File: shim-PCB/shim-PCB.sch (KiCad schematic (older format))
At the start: 23 parts, among them J1 ROMI-Encoder, J10 LineSensor, J11 LineSensor, J12 SPI, J13 Ultrasonic., J14 THING, J15 THING, J16 Conn_01x02_Female, J2 ROMI-Encoder, J3 Conn_01x19_Female, J4 ServoAnalog, J5 Conn_01x19_Female, J6 Conn_01x19_Female, J7 ROMI, J8 ROMI, J9 Conn_01x19_Female

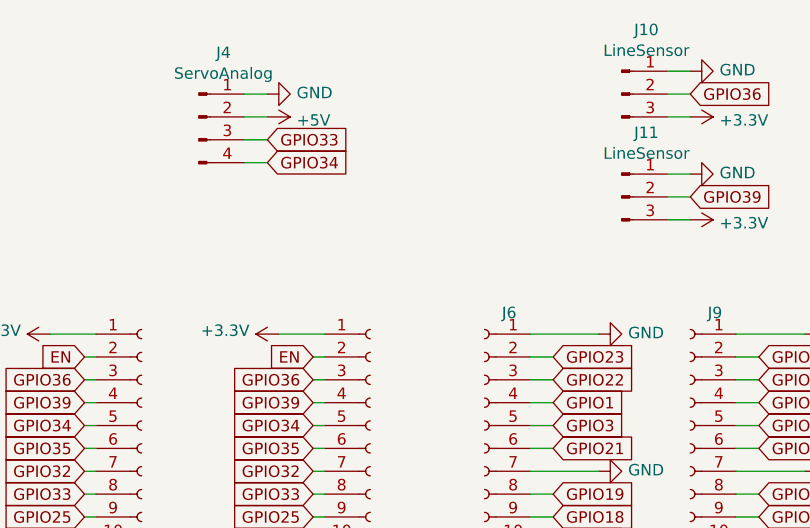
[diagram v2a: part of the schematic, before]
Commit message: Clamped analog input signal.
Fixed issue #11
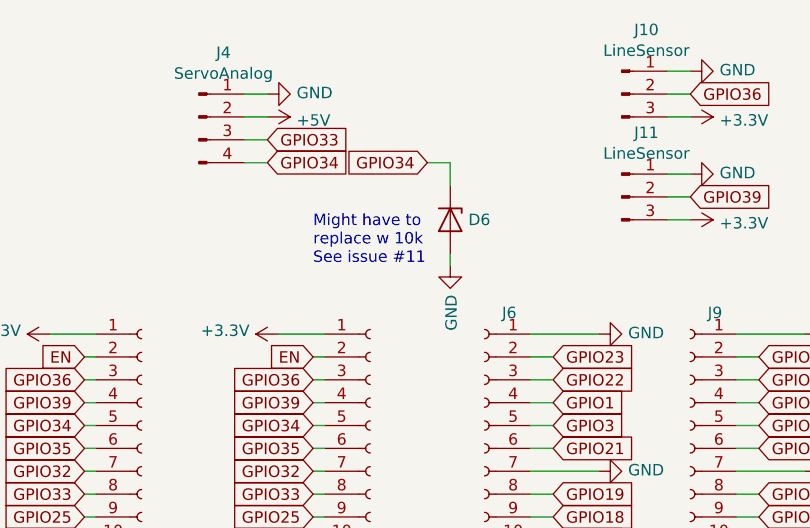
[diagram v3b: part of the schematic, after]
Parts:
- added D6: D_Zener, Diode_THT:D_DO-35_SOD27_P7.62mm_Horizontal, symbol Device:D_Zener
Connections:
- net GND: now also D6.2 (A)
- net GPIO34: now also D6.1 (K)
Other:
- note added: "Might have to\nreplace w 10k\nSee issue #11"
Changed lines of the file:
@@
 Wire Wire Line
 	4800 4650 4800 4700
+$Comp
+L Device:D_Zener D6
+U 1 1 5F32D98F
+P 2850 1550
+F 0 "D6" V 2850 1629 50  0000 L CNN
+F 1 "D_Zener" V 2895 1629 50  0001 L CNN
+F 2 "Diode_THT:D_DO-35_SOD27_P7.62mm_Horizontal" H 2850 1550 50  0001 C CNN
+F 3 "~" H 2850 1550 50  0001 C CNN
+	1    2850 1550
+	0    1    1    0
+$EndComp
+Text GLabel 2750 1300 0    50   Input ~ 0
+GPIO34
+$Comp
+L power:GND #PWR0136
+U 1 1 5F32EB84
+P 2850 1750
+F 0 "#PWR0136" H 2850 1500 50  0001 C CNN
+F 1 "GND" V 2855 1622 50  0000 R CNN
+F 2 "" H 2850 1750 50  0001 C CNN
+F 3 "" H 2850 1750 50  0001 C CNN
+	1    2850 1750
+	1    0    0    -1
+$EndComp
+Wire Wire Line
+	2750 1300 2850 1300
+Wire Wire Line
+	2850 1300 2850 1400
+Wire Wire Line
+	2850 1700 2850 1750
+Text Notes 2250 1750 0    50   ~ 0
+Might have to\nreplace w 10k\nSee issue #11
 $EndSCHEMATC
